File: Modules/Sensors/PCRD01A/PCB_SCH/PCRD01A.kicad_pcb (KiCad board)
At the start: 2 copper layers, 60.4 x 30 mm, 37 parts, among them J1 JUMP_3X2, J2 JUMP_5X2, J3 CONN1_2, J4 CONN1_2, J5 Out, P1 _, P2 _, P3 _, P4 _, Q1 BF862, U1 MAX4475, U2 AD8692

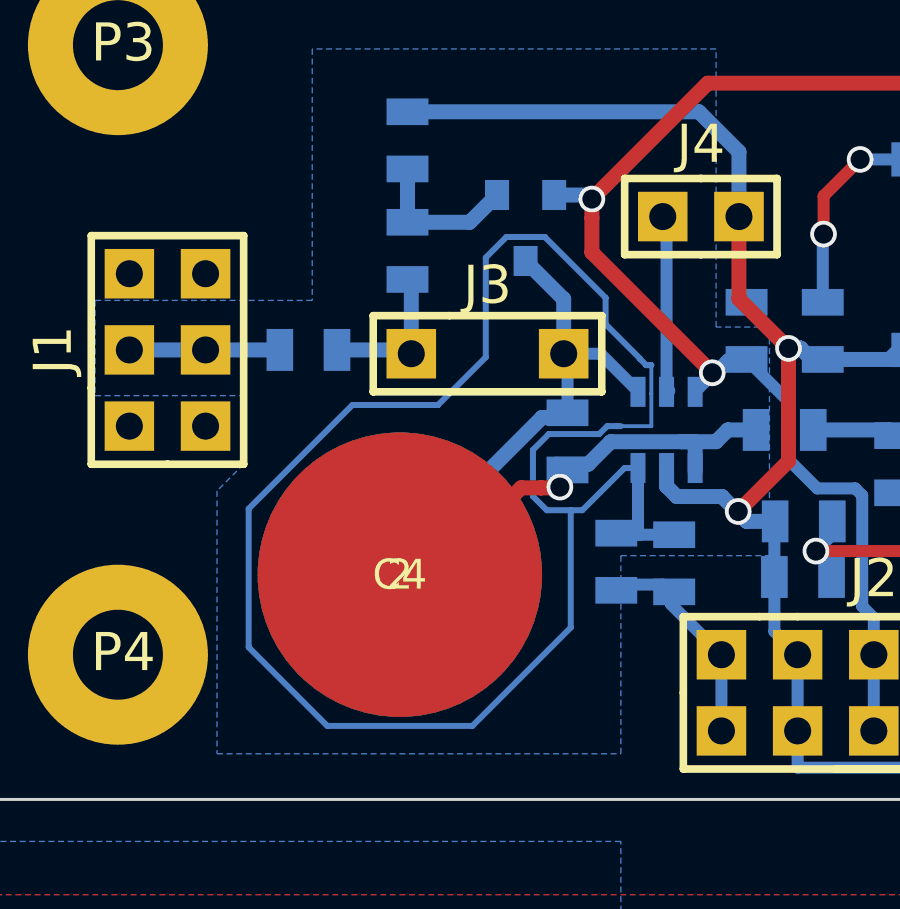
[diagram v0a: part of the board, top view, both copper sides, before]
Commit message: 
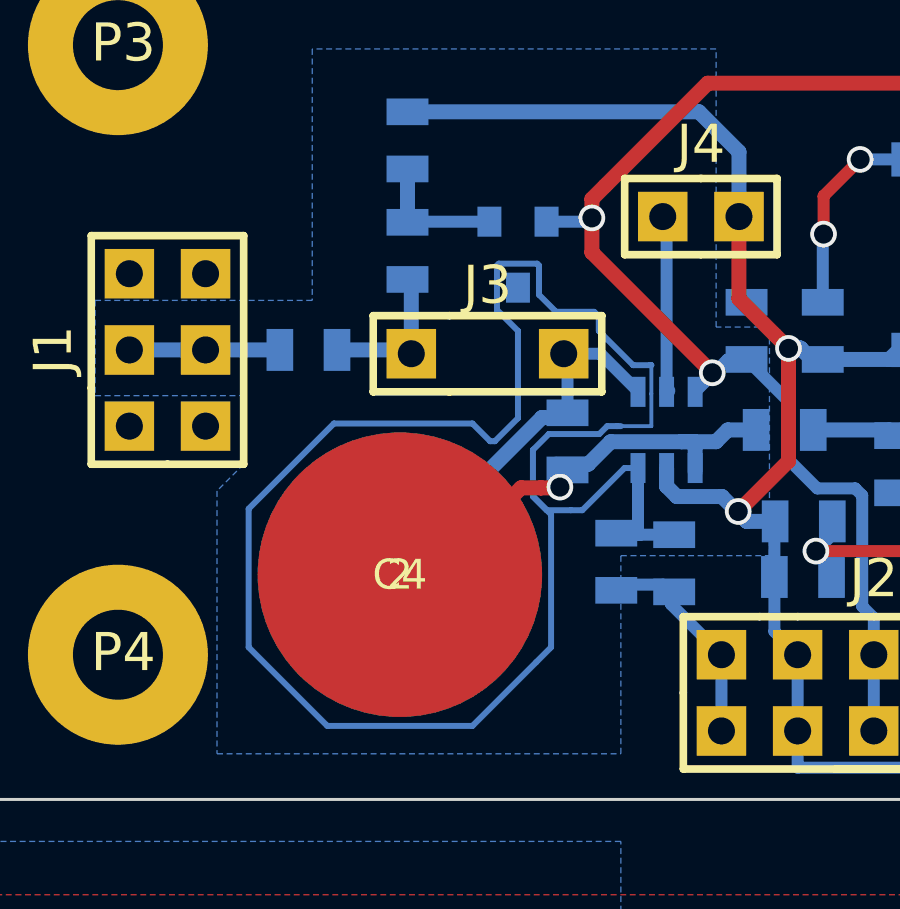
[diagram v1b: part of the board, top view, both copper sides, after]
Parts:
- moved Q1 0.92 mm to (18.4, -18.4)
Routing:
- net /A: track 16.3 -> 12.7 mm
- net Net-(C2-Pad1): track 59.8 -> 62.4 mm
- net Net-(C1-Pad1): track 5.14 -> 4.52 mm

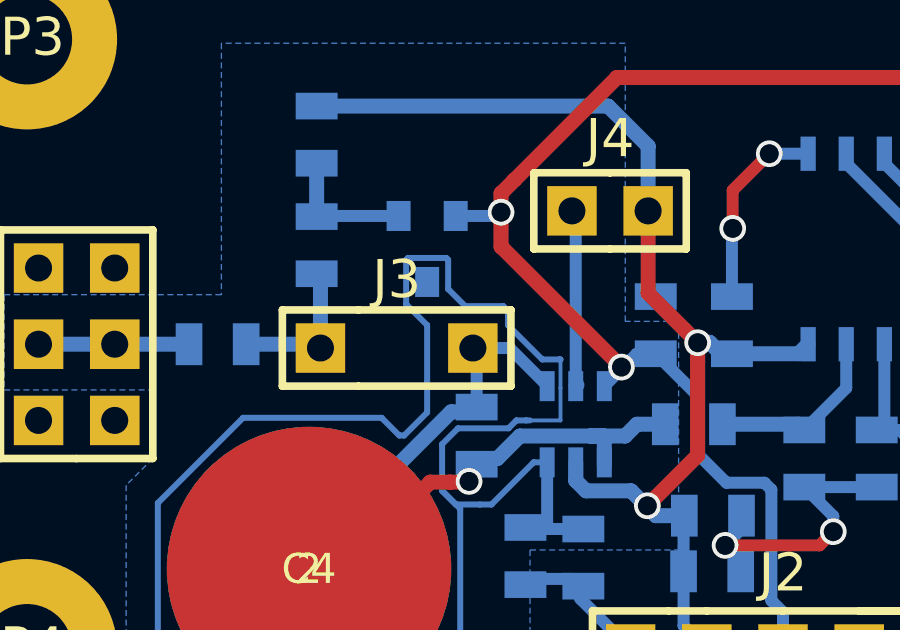
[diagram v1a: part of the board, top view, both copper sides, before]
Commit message: 
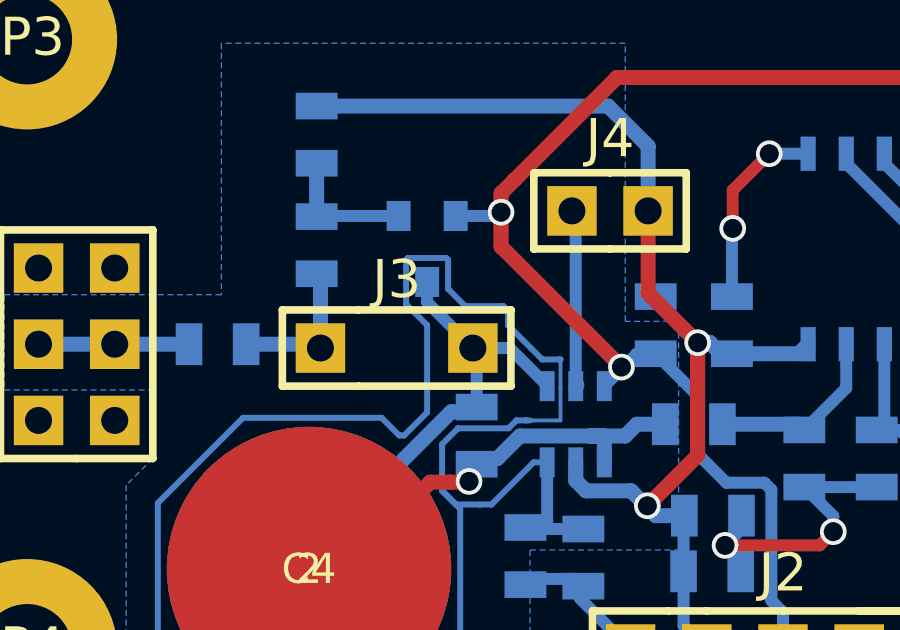
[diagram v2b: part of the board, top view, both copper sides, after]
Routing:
- net /A: track 12.7 -> 15.5 mm

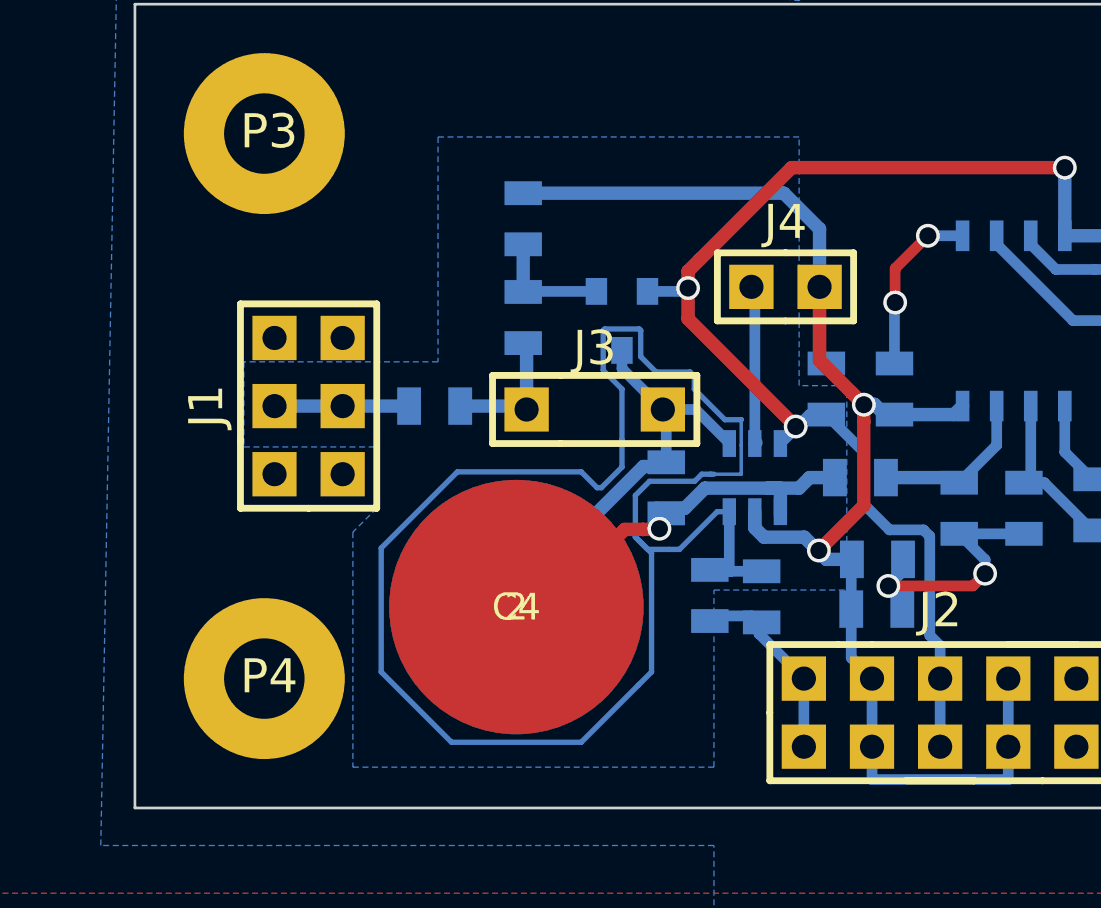
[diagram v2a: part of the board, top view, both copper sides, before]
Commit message: 
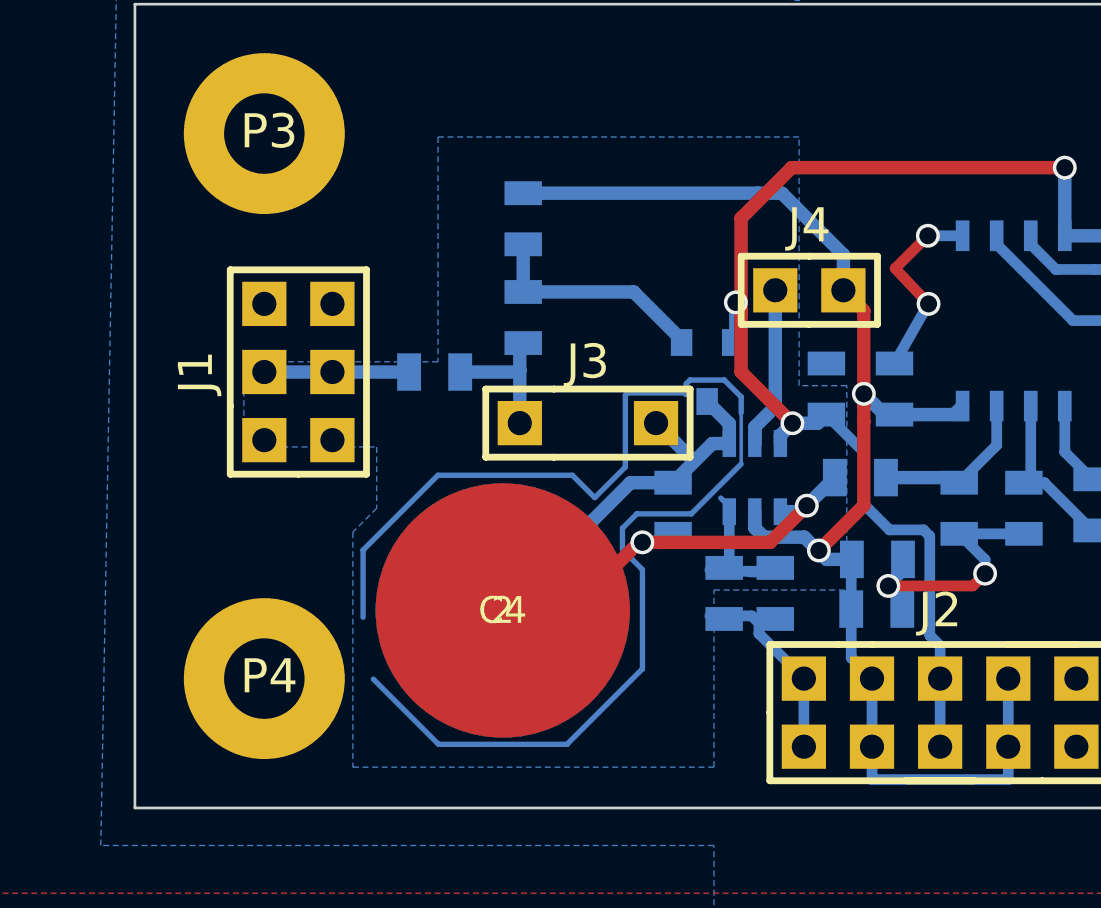
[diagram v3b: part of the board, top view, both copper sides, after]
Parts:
- moved Q1 3.70 mm to (21.6, -16.5)
- moved J1 1.33 mm to (6.35, -16.5)
- moved R2 1.27 mm to (11.4, -16.5)
- moved J4 0.90 mm to (25.4, -19.7)
- moved R4 0.80 mm to (20.3, -11.4)
- moved J3 0.57 mm to (17.1, -14.6)
- moved R3 0.54 mm to (22.2, -8.26)
- moved C2 0.52 mm to (24.1, -8.26)
- moved C4 0.52 mm to (14.0, -7.62)
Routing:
- net Net-(C2-Pad1): track 62.4 -> 5.16 mm
- net (no net): track 0.00 -> 47.7 mm
- net Net-(C1-Pad1): track 4.52 -> 8.55 mm
- net V+: track 50.6 -> 48.6 mm
- net GND: track 23.1 -> 24.0 mm
- net Net-(C4-Pad1): track 20.8 -> 20.9 mm, vias 1 -> 2

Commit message: vylepseni vedeni spoju.
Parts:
- moved R4 0.68 mm to (19.7, -11.7)
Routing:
- net Net-(C4-Pad1): track 20.9 -> 22.9 mm
- net /A: track 15.2 -> 14.5 mm

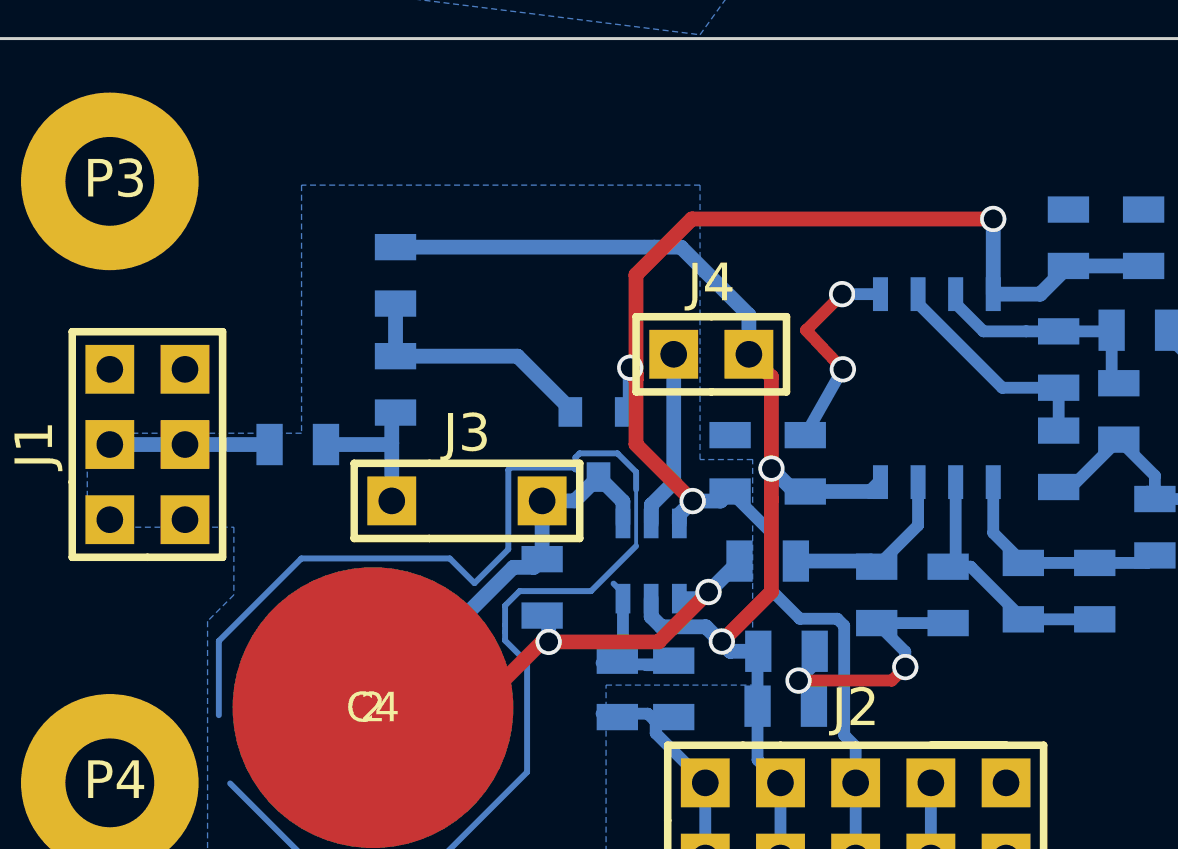
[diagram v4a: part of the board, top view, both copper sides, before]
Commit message: 
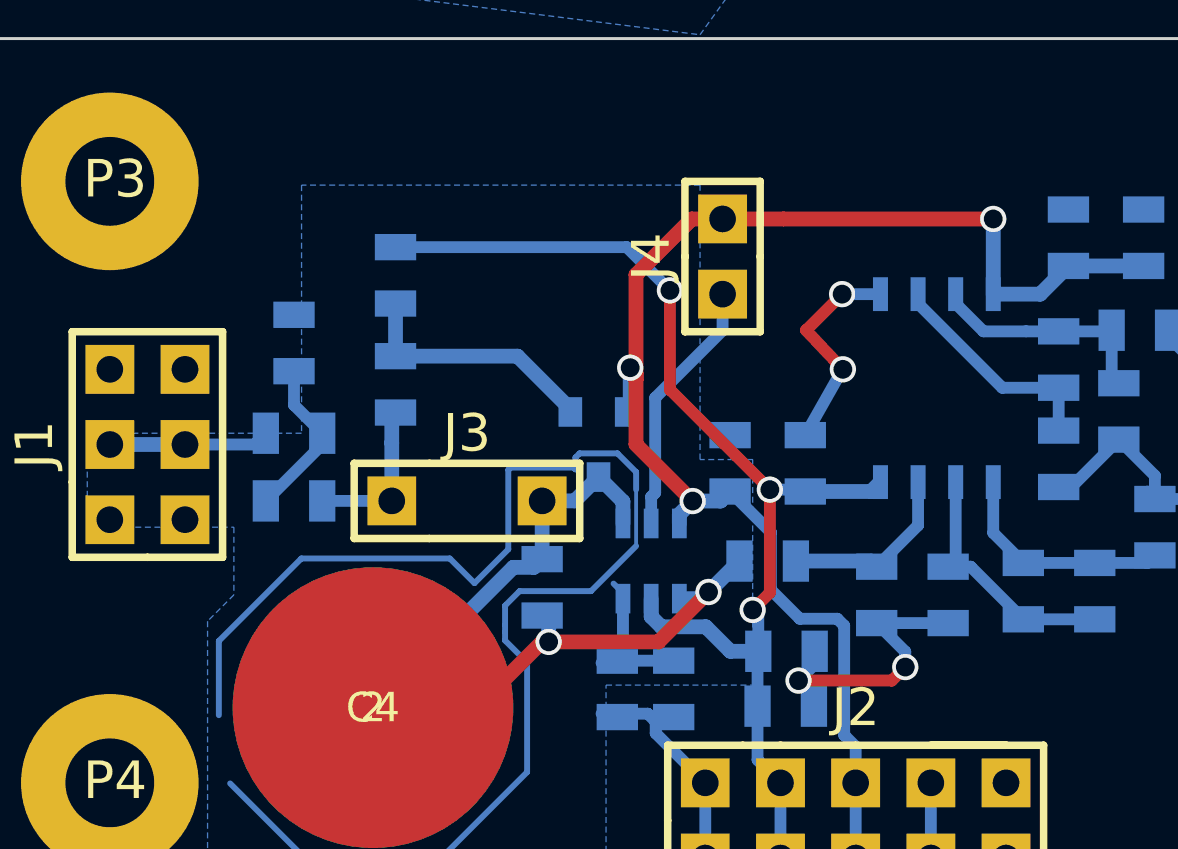
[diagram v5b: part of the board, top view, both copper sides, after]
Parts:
- added C15: 1u, Mlab_R:SMD-0805, B.Cu at (11.3, -19.9)
- added R12: 4k7, Mlab_R:SMD-0805, B.Cu at (11.3, -14.6)
- moved J4 3.19 mm to (25.7, -22.9), turned to 90 degrees
- moved R2 0.40 mm to (11.3, -16.9)
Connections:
- J4 pad 2: V- -> V+
- R2 pad 1: /K -> Net-(C15-Pad1)
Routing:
- net Net-(C15-Pad1): track 0.00 -> 5.57 mm
- net /#SHDN: track 6.03 -> 8.75 mm
- net V+: track 48.6 -> 50.7 mm
- net V-: track 52.1 -> 50.6 mm, vias 2 -> 3

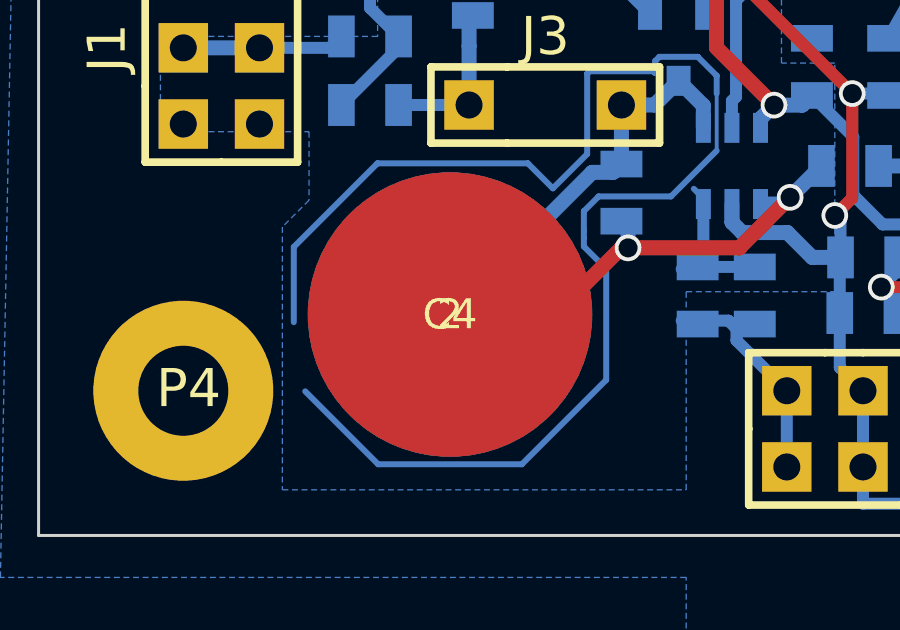
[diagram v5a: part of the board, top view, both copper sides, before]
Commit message: 
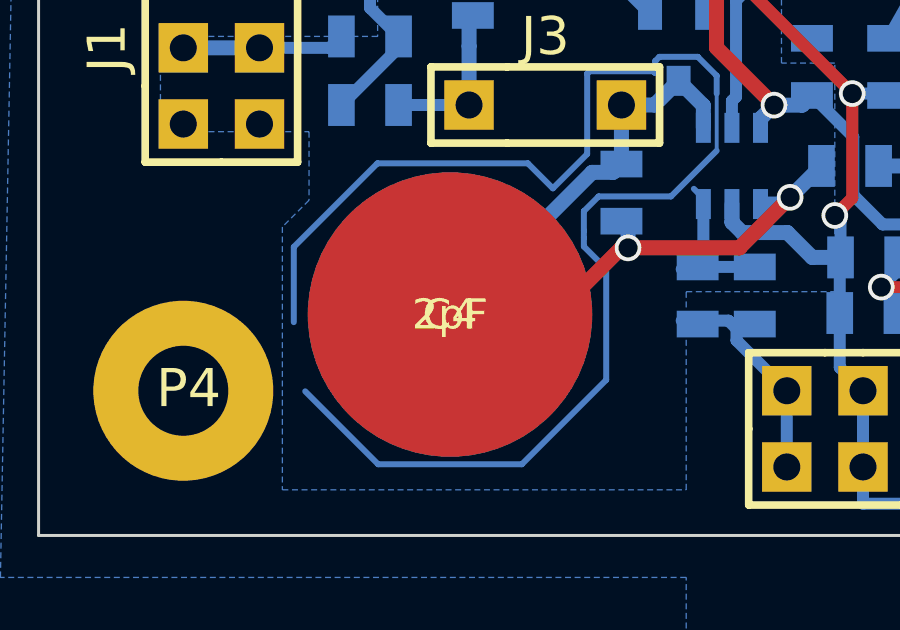
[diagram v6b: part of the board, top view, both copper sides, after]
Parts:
- C1: value 4M7 -> 4u7
- C11: value 510 -> 510pF
- C12: value 620 -> 620pF
- C13: value 100 -> 100pF
- C14, C8: value 330k -> 330nF
- C4: value 2 -> 2pF

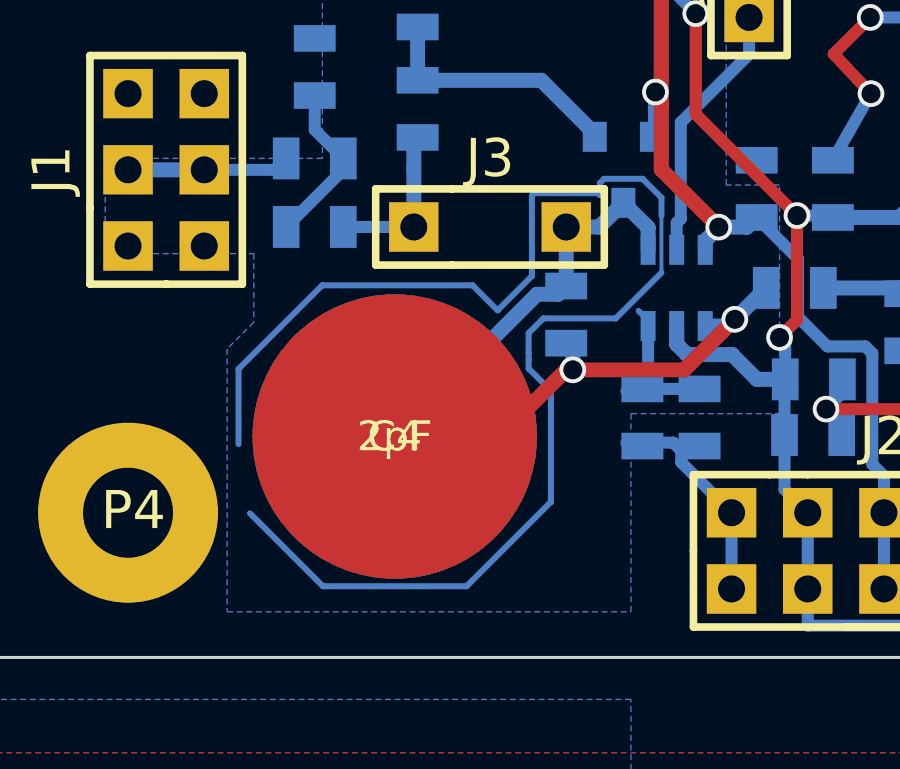
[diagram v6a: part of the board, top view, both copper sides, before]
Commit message: pripojeni guard ringu.
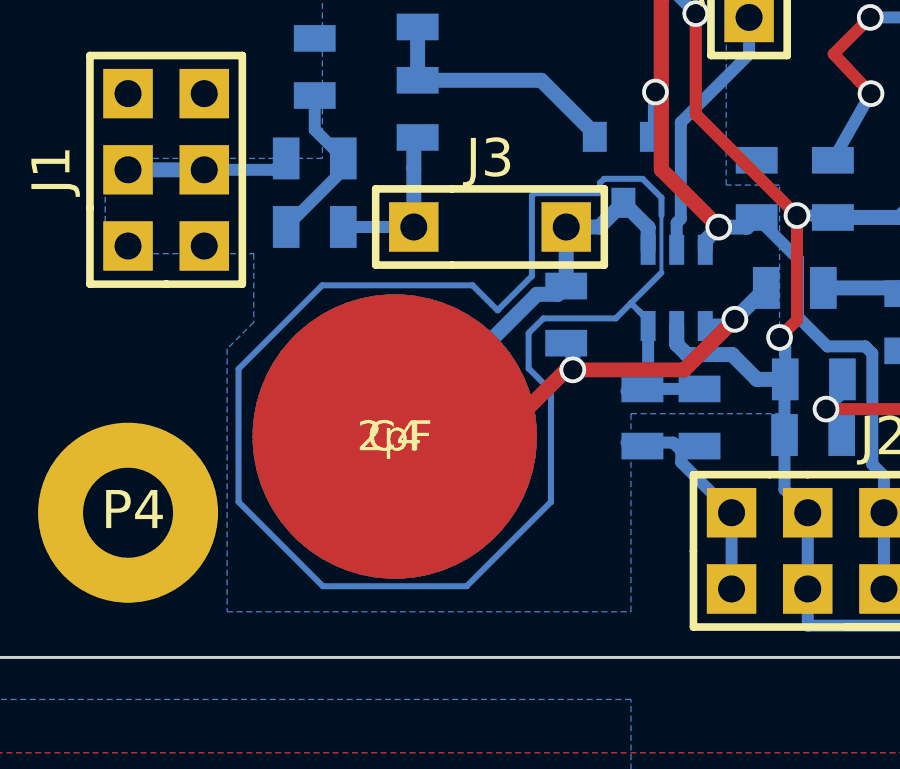
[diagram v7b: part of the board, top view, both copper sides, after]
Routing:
- net Net-(C2-Pad1): track 5.51 -> 56.5 mm
- net (no net): track 47.9 -> 0.00 mm

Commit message: posunuti rezistoru.
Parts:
- moved R2 1.10 mm to (10.3, -16.5)
- moved C15 0.72 mm to (11.3, -19.2)
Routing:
- net Net-(C15-Pad1): track 5.57 -> 4.04 mm
- net /+Ubias: track 5.43 -> 4.24 mm
